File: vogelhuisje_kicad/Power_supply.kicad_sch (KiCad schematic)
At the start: 9 parts, among them J1 Conn_01x02_Female, J2 Conn_01x02, J3 USB_C_Receptacle_USB2.0, P1 TP4056breakout, P2 GenericBoostConverter, Q1 Q_PMOS_GSD

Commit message: PCB done with version 1
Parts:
- added R1: -, Resistor_THT:R_Axial_DIN0207_L6.3mm_D2.5mm_P7.62mm_Horizontal, symbol Device:R
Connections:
- net GND: now also P1.6 (OUT-), P2.2 (GND), R2.2
- net turn_on_boost_converter: now also R1.1
- net at D2.1 (K), Q1.1 (G): now also R1.2
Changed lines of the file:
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@@
   (junction (at 91.44 62.23) (diameter 0) (color 0 0 0 0)
+  )
+  (junction (at 100.33 62.23) (diameter 0) (color 0 0 0 0)
   )
   (junction (at 106.68 44.45) (diameter 0) (color 0 0 0 0)
@@
     (stroke (width 0) (type default) (color 0 0 0 0))
   )
+  (wire (pts (xy 91.44 62.23) (xy 100.33 62.23))
+    (stroke (width 0) (type default) (color 0 0 0 0))
+  )
   (wire (pts (xy 91.44 44.45) (xy 97.79 44.45))
     (stroke (width 0) (type default) (color 0 0 0 0))
@@
     (stroke (width 0) (type default) (color 0 0 0 0))
   )
-  (wire (pts (xy 91.44 62.23) (xy 123.19 62.23))
-    (stroke (width 0) (type default) (color 0 0 0 0))
-  )
   (wire (pts (xy 97.79 52.07) (xy 97.79 54.61))
+    (stroke (width 0) (type default) (color 0 0 0 0))
+  )
+  (wire (pts (xy 100.33 62.23) (xy 123.19 62.23))
     (stroke (width 0) (type default) (color 0 0 0 0))
   )
@@
     (pin "1")
   )
+  (symbol (lib_id "power:GND") (at 100.33 62.23 0) (unit 1)
+    (in_bom yes) (on_board yes) (fields_autoplaced)
+    (property "Reference" "#PWR0104" (id 0) (at 100.33 68.58 0)
+      (effects (font (size 1.27 1.27)) hide)
+    )
+    (property "Value" "GND" (id 1) (at 100.33 67.31 0))
+    (property "Footprint" "" (id 2) (at 100.33 62.23 0)
+      (effects (font (size 1.27 1.27)) hide)
+    )
+    (property "Datasheet" "" (id 3) (at 100.33 62.23 0)
+      (effects (font (size 1.27 1.27)) hide)
+    )
+    (pin "1")
+  )
   (symbol (lib_id "Device:D_Schottky") (at 97.79 48.26 90) (unit 1)
     (in_bom yes) (on_board yes) (fields_autoplaced)
@@
       (effects (font (size 1.27 1.27)) hide)
     )
+    (pin "1")
+    (pin "2")
+  )
+  (symbol (lib_id "Device:R") (at 106.68 31.75 0) (unit 1)
+    (in_bom yes) (on_board yes)
+    (property "Reference" "R1" (id 0) (at 108.458 30.5816 0)
+      (effects (font (size 1.27 1.27)) (justify left))
+    )
+    (property "Value" "-" (id 1) (at 108.458 32.893 0)
+      (effects (font (size 1.27 1.27)) (justify left))
+    )
+    (property "Footprint" "Resistor_THT:R_Axial_DIN0207_L6.3mm_D2.5mm_P7.62mm_Horizontal" (id 2) (at 104.902 31.75 90)
+      (effects (font (size 1.27 1.27)) hide)
+    )
+    (property "Datasheet" "~" (id 3) (at 106.68 31.75 0)
+      (effects (font (size 1.27 1.27)) hide)
+    )

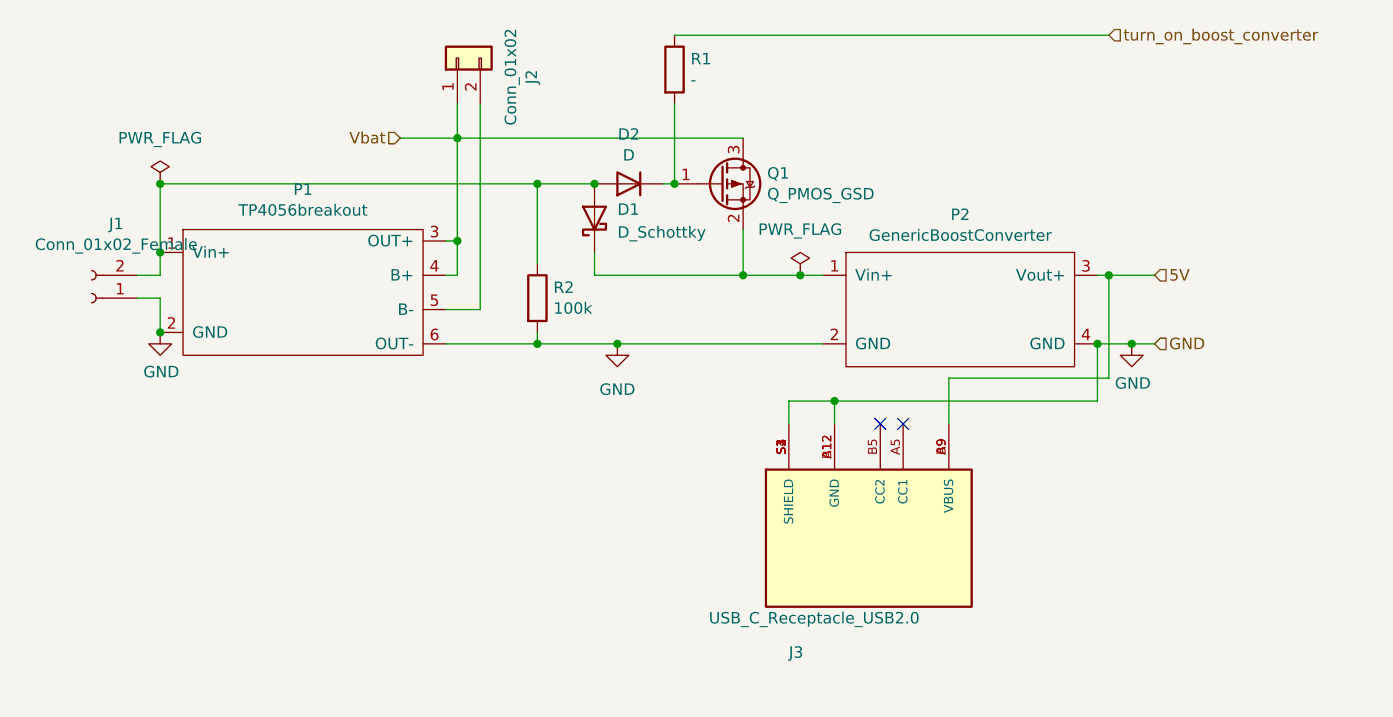
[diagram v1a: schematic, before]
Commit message: Kicad Changes Tadjiro
Board now supports 3 lipo cells and a motion sensor.
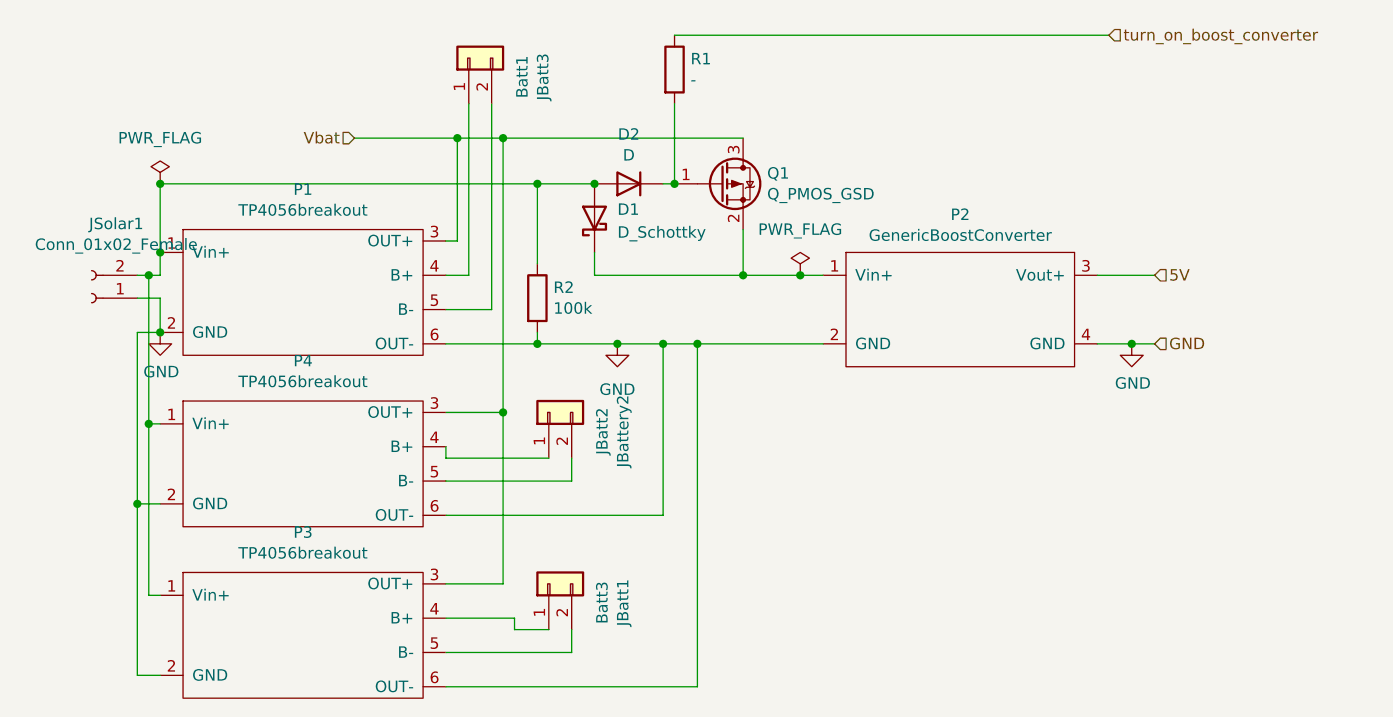
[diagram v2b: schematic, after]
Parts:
- removed J3: USB_C_Receptacle_USB2.0, GCT_USB4125-GF-A-0190_REVA2, symbol usbC:USB4125-GF-A-0190_REVA2
- added JBatt1: Batt3, Connector_JST:JST_PH_B2B-PH-K_1x02_P2.00mm_Vertical, symbol Connector_Generic:Conn_01x02
- added JBattery2: JBatt2, Connector_JST:JST_PH_B2B-PH-K_1x02_P2.00mm_Vertical, symbol Connector_Generic:Conn_01x02
- added P3, P4: TP4056breakout, components:TP4056breakout, symbol TP4056-breakout:TP4056breakout
- D1: footprint Diode_SMD:D_SMB_Handsoldering -> Diode_THT:D_DO-41_SOD81_P3.81mm_Vertical_KathodeUp
- JBatt3: renamed from J2; value Conn_01x02 -> Batt1
- Q1: footprint Package_TO_SOT_SMD:SOT-23 -> Package_TO_SOT_THT:TO-220-3_Vertical
- renumbered J1 to JSolar1
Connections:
- net GND: now also P3.2 (GND), P3.6 (OUT-), P4.2 (GND), P4.6 (OUT-)
- net Vbat: now also P3.3 (OUT+), P4.3 (OUT+); no longer JBatt3.1 (Pin_1), P1.4 (B+)
- net at D1.2 (A), D2.2 (A), JSolar1.2 (Pin_2)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: now also P3.1 (Vin+), P4.1 (Vin+)
- new net: JBatt3.1 (Pin_1), P1.4 (B+)
- new net: JBattery2.1 (Pin_1), P4.4 (B+)
- new net: JBattery2.2 (Pin_2), P4.5 (B-)
- new net: JBatt1.1 (Pin_1), P3.4 (B+)
- new net: JBatt1.2 (Pin_2), P3.5 (B-)
- no-connect marks 2 -> 0
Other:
- moved on the sheet: JBatt3
